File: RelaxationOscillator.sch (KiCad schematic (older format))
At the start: 27 parts, among them P202 CONN_2, P203 CONN_2, SW201 SPST, U201 LM358N

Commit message: Updated schematic and moved files to new location
Corrected errors in the schematic which will affect the PCB. PCB not
changed yet. Updated resistor and cap values and changed amp type to
comply with the simulations. The CAD A wien-bridge PCB will not
oscillate. The relaxation oscillator will oscillate but the new values
are required. The new schematic adds new components to the circuit which
need putting into the PCB.
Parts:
- removed U201: LM358N, symbol LM358N
- added R217: 20k, ~, symbol R
- added R218: 1k, ~, symbol R
- added U201: TL072, symbol TL072
- C201: value 2.2n -> 10n
- C204, C205, C206: value 10uF -> 100uF
- R201, R202, R203, R204: value 100k -> 1k
- R205: value 100k -> 10k
- R206, R207, R208: value 100k -> 20k
- R209, R210: value 20k -> 6.8k
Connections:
- net GND: now also U201.4 (V-), U201.4 (V-); no longer C202.2, R210.2
- net IN1+: now also C201.1, U201.2 (-); no longer C206.1, R203.2, R204.1
- net IN1-: no longer C201.1, R207.1
- net IN2+: now also R205.2, R208.1, U201.6 (-); no longer C202.1, R209.2, R210.1
- net IN2-: no longer R205.2, R208.1
- net SINUSOID: now also R218.2, U201.7; no longer R208.2
- net SQUARE: now also U201.1
- net VCC: now also U201.8 (V+), U201.8 (V+)
- net at C205.1, R201.2, R202.1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: now also C202.2, R210.2
- new net: R207.1, R217.2, U201.3 (+)
- new net: C202.1, R209.2, R210.1, U201.5 (+)
- new net: C206.1, R203.2, R204.1, R217.1
- new net: R208.2, R218.1
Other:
- note added: "TL072 would be a better alternative to the LM358 but with the same pinout."
- note removed: "TL072 would be a better alternative to the LM358 but with the same pinout. change to TL072 part"
- moved on the sheet: C201, C202, C205, C206, R201, R202, R203, R204, R205, R208, R210

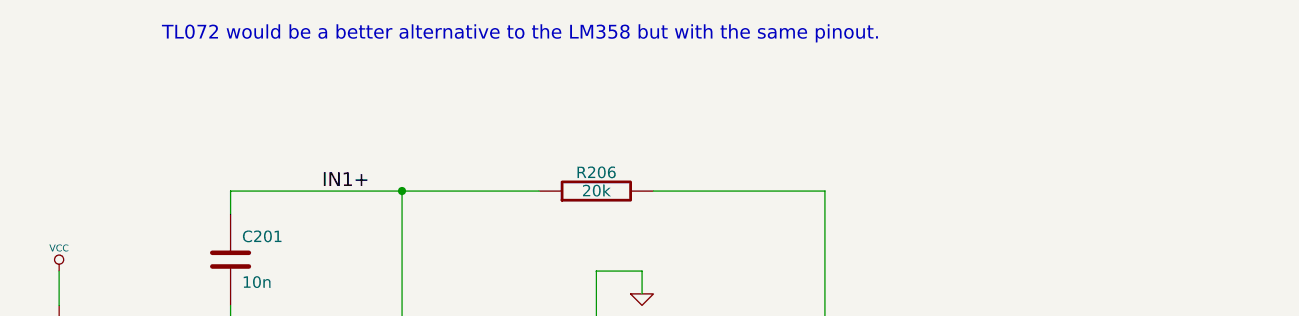
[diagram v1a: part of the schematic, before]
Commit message: PCB updated from schema. Using new Kicad version
Updated the PCB with the schematic updates. Using the newer kicad
version for windows. 7-7-2013 BZR 4022 -stable
The old PCB file has been updated to the new version.
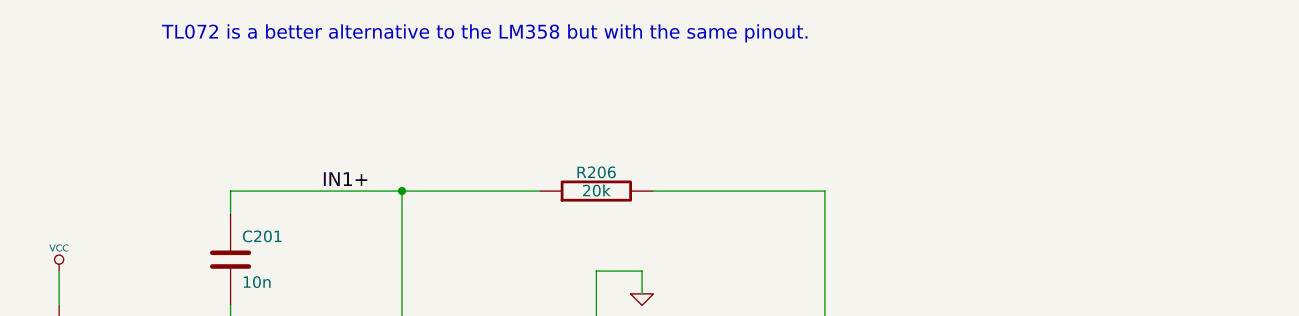
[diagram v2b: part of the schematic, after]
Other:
- note added: "TL072 is a better alternative to the LM358 but with the same pinout."
- note removed: "TL072 would be a better alternative to the LM358 but with the same pinout."
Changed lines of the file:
@@
 Sheet 2 3
 Title ""
-Date "11 mar 2014"
+Date "16 mar 2014"
 Rev ""
 Comp ""
@@
 $EndComp
 $Comp
-L GND #PWR214
+L GND #PWR01
 U 1 1 52FBE795
 P 8000 5400
-F 0 "#PWR214" H 8000 5400 30  0001 C CNN
+F 0 "#PWR01" H 8000 5400 30  0001 C CNN
 F 1 "GND" H 8000 5330 30  0001 C CNN
 F 2 "" H 8000 5400 60  0001 C CNN
@@
 $EndComp
 $Comp
-L GND #PWR213
+L GND #PWR02
 U 1 1 52FBE703
 P 7600 3350
-F 0 "#PWR213" H 7600 3350 30  0001 C CNN
+F 0 "#PWR02" H 7600 3350 30  0001 C CNN
 F 1 "GND" H 7600 3280 30  0001 C CNN
 F 2 "" H 7600 3350 60  0001 C CNN
@@
 $EndComp
 Text Notes 4300 950  0    60   ~ 0
-TL072 would be a better alternative to the LM358 but with the same pinout.
-$Comp
-L GND #PWR203
+TL072 is a better alternative to the LM358 but with the same pinout.
+$Comp
+L GND #PWR03
 U 1 1 52F7B719
 P 3100 3300
-F 0 "#PWR203" H 3100 3300 30  0001 C CNN
+F 0 "#PWR03" H 3100 3300 30  0001 C CNN
 F 1 "GND" H 3100 3230 30  0001 C CNN
 F 2 "" H 3100 3300 60  0001 C CNN
@@
 $EndComp
 $Comp
-L VCC #PWR202
+L VCC #PWR04
 U 1 1 52F7B718
 P 3100 2150
-F 0 "#PWR202" H 3100 2250 30  0001 C CNN
+F 0 "#PWR04" H 3100 2250 30  0001 C CNN
 F 1 "VCC" H 3100 2250 30  0000 C CNN
 F 2 "" H 3100 2150 60  0001 C CNN
@@
 SINUSOID
 $Comp
-L GND #PWR201
+L GND #PWR05
 U 1 1 52F78702
 P 1300 3300
-F 0 "#PWR201" H 1300 3300 30  0001 C CNN
+F 0 "#PWR05" H 1300 3300 30  0001 C CNN
 F 1 "GND" H 1300 3230 30  0001 C CNN
 F 2 "" H 1300 3300 60  0001 C CNN
@@
 $EndComp
 $Comp
-L GND #PWR216
+L GND #PWR06
 U 1 1 52F78634
 P 8900 5600
-F 0 "#PWR216" H 8900 5600 30  0001 C CNN
+F 0 "#PWR06" H 8900 5600 30  0001 C CNN
 F 1 "GND" H 8900 5530 30  0001 C CNN
 F 2 "" H 8900 5600 60  0001 C CNN
@@
 $EndComp
 $Comp
-L GND #PWR215
+L GND #PWR07
 U 1 1 52F7861B
 P 8400 3500
-F 0 "#PWR215" H 8400 3500 30  0001 C CNN
+F 0 "#PWR07" H 8400 3500 30  0001 C CNN
 F 1 "GND" H 8400 3430 30  0001 C CNN
 F 2 "" H 8400 3500 60  0001 C CNN
@@
 SQUARE
 $Comp
-L GND #PWR205
+L GND #PWR08
 U 1 1 52F7847B
 P 3100 6550
-F 0 "#PWR205" H 3100 6550 30  0001 C CNN
+F 0 "#PWR08" H 3100 6550 30  0001 C CNN
 F 1 "GND" H 3100 6480 30  0001 C CNN
 F 2 "" H 3100 6550 60  0001 C CNN
@@
 $EndComp
 $Comp
-L VCC #PWR204
+L VCC #PWR09
 U 1 1 52F78476
 P 3100 4300
-F 0 "#PWR204" H 3100 4400 30  0001 C CNN
+F 0 "#PWR09" H 3100 4400 30  0001 C CNN
 F 1 "VCC" H 3100 4400 30  0000 C CNN
 F 2 "" H 3100 4300 60  0001 C CNN
@@
 $EndComp
 $Comp
-L GND #PWR211
+L GND #PWR010
 U 1 1 52F78463
 P 6500 4000
-F 0 "#PWR211" H 6500 4000 30  0001 C CNN
+F 0 "#PWR010" H 6500 4000 30  0001 C CNN
 F 1 "GND" H 6500 3930 30  0001 C CNN
 F 2 "" H 6500 4000 60  0001 C CNN
@@
 $EndComp
 $Comp
-L VCC #PWR212
+L VCC #PWR011
 U 1 1 52F78447
 P 6500 5050
-F 0 "#PWR212" H 6500 5150 30  0001 C CNN
+F 0 "#PWR011" H 6500 5150 30  0001 C CNN
 F 1 "VCC" H 6500 5150 30  0000 C CNN
 F 2 "" H 6500 5050 60  0001 C CNN
@@
 $EndComp
 $Comp
-L GND #PWR208
+L GND #PWR012
 U 1 1 52F77FA3
 P 4600 2300
-F 0 "#PWR208" H 4600 2300 30  0001 C CNN
+F 0 "#PWR012" H 4600 2300 30  0001 C CNN
 F 1 "GND" H 4600 2230 30  0001 C CNN
 F 2 "" H 4600 2300 60  0001 C CNN
@@
 $EndComp
 $Comp
-L GND #PWR207
+L GND #PWR013
 U 1 1 52F77F1E
 P 3850 3500
-F 0 "#PWR207" H 3850 3500 30  0001 C CNN
+F 0 "#PWR013" H 3850 3500 30  0001 C CNN
 F 1 "GND" H 3850 3430 30  0001 C CNN
 F 2 "" H 3850 3500 60  0001 C CNN
@@
 $EndComp
 $Comp
-L VCC #PWR206
+L VCC #PWR014
 U 1 1 52F77F13
 P 3850 1950
-F 0 "#PWR206" H 3850 2050 30  0001 C CNN
+F 0 "#PWR014" H 3850 2050 30  0001 C CNN
 F 1 "VCC" H 3850 2050 30  0000 C CNN
 F 2 "" H 3850 1950 60  0001 C CNN
@@
 $EndComp
 $Comp
-L VCC #PWR210
+L VCC #PWR015
 U 1 1 52F77D36
 P 6500 3150
-F 0 "#PWR210" H 6500 3250 30  0001 C CNN
+F 0 "#PWR015" H 6500 3250 30  0001 C CNN
 F 1 "VCC" H 6500 3250 30  0000 C CNN
 F 2 "" H 6500 3150 60  0001 C CNN
@@
 $EndComp
 $Comp
-L GND #PWR209
+L GND #PWR016
 U 1 1 52F77D02
 P 6400 2050
-F 0 "#PWR209" H 6400 2050 30  0001 C CNN
+F 0 "#PWR016" H 6400 2050 30  0001 C CNN
 F 1 "GND" H 6400 1980 30  0001 C CNN
 F 2 "" H 6400 2050 60  0001 C CNN
